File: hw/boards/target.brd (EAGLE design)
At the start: 25.4 x 25.4 mm, 21 parts, among them T1 771-BC847BS-T/R, U1 579-MCP1703T-3002ECB, U2 771-LPC824M201JDH20J, U4 579-MCP6291T-E/OT, X1 798-DF134P125V20

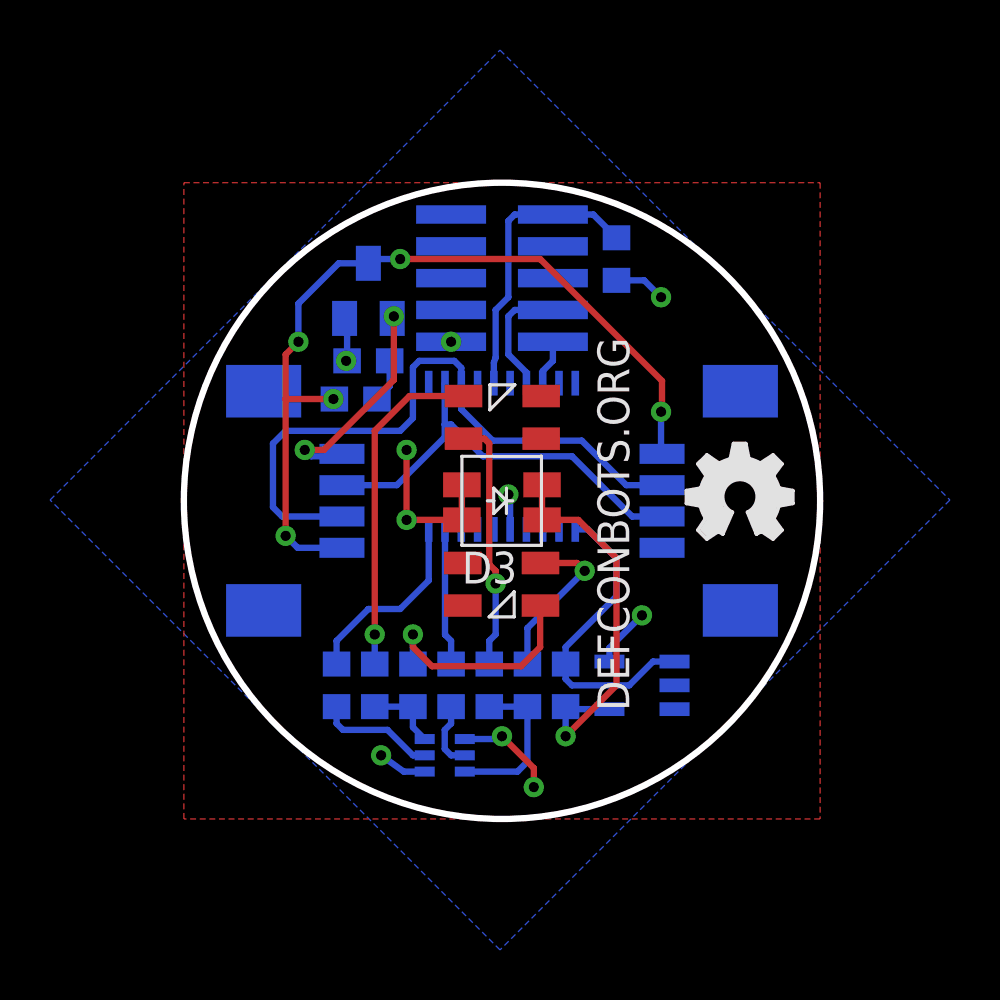
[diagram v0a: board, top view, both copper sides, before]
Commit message: Cleanup some routing. Fix some part numbers
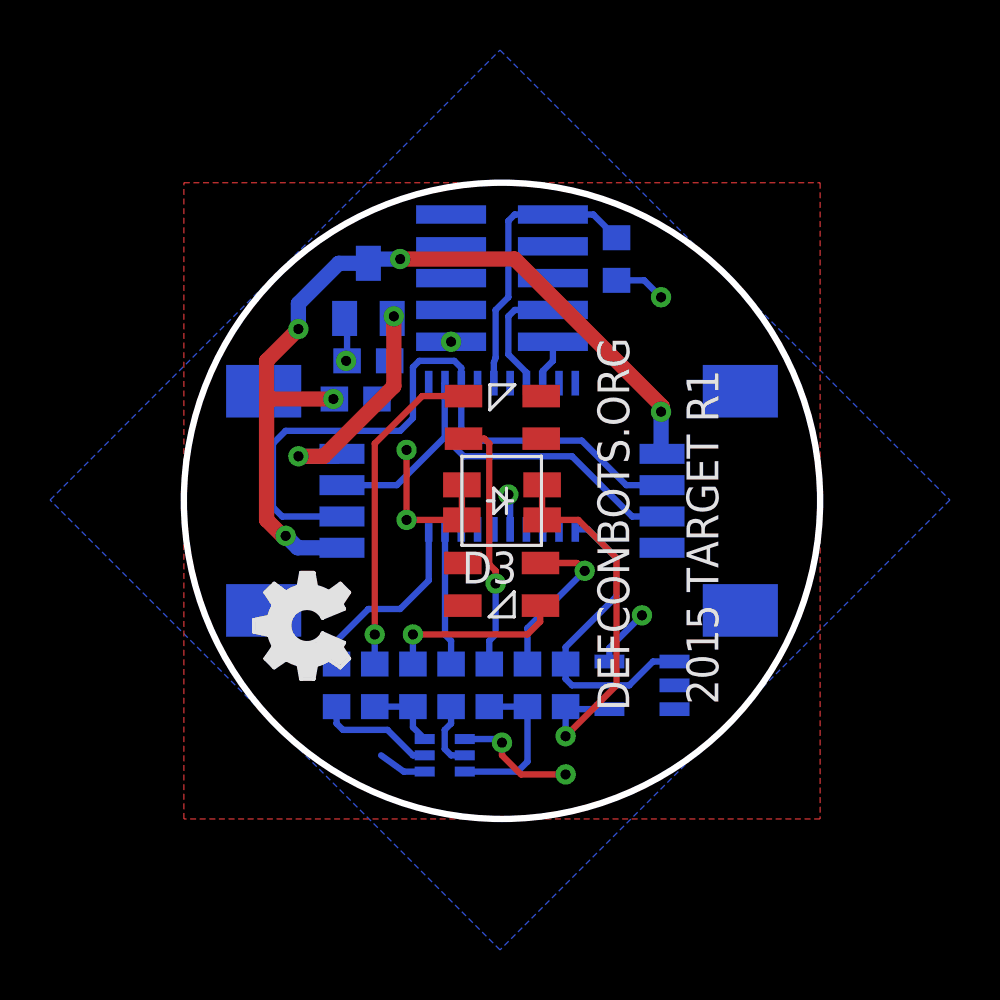
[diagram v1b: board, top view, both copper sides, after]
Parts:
- moved LOGO2 14.6 mm to (6.60, 5.59), turned to 90 degrees
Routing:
- net N$3: track 9.07 -> 7.12 mm
- net GND: track 23.2 -> 24.7 mm, vias 7 -> 6
- net VIN: track 34.3 -> 35.2 mm
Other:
- board text added: "2015 TARGET R1"
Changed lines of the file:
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@@
 <plain>
 <circle x="12.7" y="12.7" radius="12.7" width="0.254" layer="20"/>
-<text x="17.78" y="4.318" size="1.27" layer="21" rot="R90">DEFCONBOTS.ORG</text>
+<text x="17.78" y="4.318" size="1.27" layer="21" font="vector" rot="R90">DEFCONBOTS.ORG</text>
+<text x="21.336" y="4.572" size="1.27" layer="21" font="vector" rot="R90">2015 TARGET R1</text>
 </plain>
 <attributes>
@@
 </element>
 <element name="JP2" library="torpedo" package="FTSH-105-01-XXX-DV-K" value="FTSH-105-01-L" x="12.7" y="21.59" rot="MR90"/>
-<element name="LOGO2" library="ohw-logo" package="OSHW_FILLX150_NOTEXT" value="OSHW_LOGO_FILLX0150-NT" x="20.066" y="11.176"/>
+<element name="LOGO2" library="ohw-logo" package="OSHW_FILLX150_NOTEXT" value="OSHW_LOGO_FILLX0150-NT" x="6.604" y="5.588" rot="R90"/>
 <element name="R1" library="rcl" package="R0603" value="71-CRCW0603-5.6-E3" x="13.716" y="5.334" rot="MR90"/>
 <element name="R11" library="rcl" package="R0603" value="71-CRCW060368R0FKEB" x="9.144" y="5.334" rot="MR90"/>
@@
 <wire x1="9.614" y1="1.89" x2="8.778" y2="1.89" width="0.254" layer="16"/>
 <wire x1="8.778" y1="1.89" x2="7.874" y2="2.54" width="0.254" layer="16"/>
-<via x="7.874" y="2.54" extent="1-16" drill="0.4064"/>
 <wire x1="11.0998" y1="11.938" x2="8.89" y2="11.938" width="0.254" layer="1"/>
 <via x="8.89" y="11.938" extent="1-16" drill="0.4064"/>
@@
 <wire x1="11.0998" y1="11.938" x2="11.0998" y2="13.338" width="0.254" layer="1"/>
 <wire x1="11.214" y1="3.19" x2="12.588" y2="3.19" width="0.254" layer="16"/>
-<wire x1="12.588" y1="3.19" x2="12.7" y2="3.302" width="0.254" layer="16"/>
-<via x="12.7" y="3.302" extent="1-16" drill="0.4064"/>
-<via x="13.97" y="1.27" extent="1-16" drill="0.4064"/>
-<wire x1="12.7" y1="3.302" x2="13.97" y2="2.032" width="0.254" layer="1"/>
-<wire x1="13.97" y1="2.032" x2="13.97" y2="1.27" width="0.254" layer="1"/>
+<wire x1="12.588" y1="3.19" x2="12.7" y2="3.048" width="0.254" layer="16"/>
+<via x="12.7" y="3.048" extent="1-16" drill="0.4064"/>
+<via x="15.24" y="1.778" extent="1-16" drill="0.4064"/>
+<wire x1="12.7" y1="3.048" x2="12.7" y2="2.54" width="0.254" layer="1"/>
+<wire x1="12.7" y1="2.54" x2="13.462" y2="1.778" width="0.254" layer="1"/>
+<wire x1="13.462" y1="1.778" x2="15.24" y2="1.778" width="0.254" layer="1"/>
 <wire x1="8.89" y1="14.732" x2="8.89" y2="11.938" width="0.254" layer="1"/>
-<wire x1="8.382" y1="17.526" x2="8.382" y2="20.066" width="0.254" layer="1"/>
-<wire x1="5.588" y1="14.732" x2="8.382" y2="17.526" width="0.254" layer="1"/>
-<wire x1="4.826" y1="14.732" x2="5.588" y2="14.732" width="0.254" layer="1"/>
-<wire x1="5.08" y1="14.478" x2="4.826" y2="14.732" width="0.254" layer="16"/>
-<wire x1="6.096" y1="14.478" x2="5.08" y2="14.478" width="0.254" layer="16"/>
+<wire x1="8.382" y1="17.272" x2="8.382" y2="20.066" width="0.6096" layer="1"/>
+<wire x1="5.588" y1="14.478" x2="8.382" y2="17.272" width="0.6096" layer="1"/>
+<wire x1="4.572" y1="14.478" x2="5.588" y2="14.478" width="0.6096" layer="1"/>
+<wire x1="6.096" y1="14.478" x2="4.572" y2="14.478" width="0.6096" layer="16"/>
 <wire x1="6.096" y1="14.478" x2="6.31" y2="14.575" width="0.254" layer="16"/>
 <via x="8.382" y="20.066" extent="1-16" drill="0.4064"/>
-<via x="4.826" y="14.732" extent="1-16" drill="0.4064"/>
+<via x="4.572" y="14.478" extent="1-16" drill="0.4064"/>
 <wire x1="7.708" y1="16.764" x2="8.216" y2="17.272" width="0.254" layer="16"/>
 <wire x1="8.216" y1="17.272" x2="8.216" y2="18.288" width="0.254" layer="16"/>
@@
 <contactref element="JP1" pad="1"/>
 <contactref element="X1" pad="1"/>
-<wire x1="6.31" y1="10.825" x2="4.542" y2="10.825" width="0.254" layer="16"/>
-<wire x1="4.542" y1="10.825" x2="4.064" y2="11.303" width="0.254" layer="16"/>
+<wire x1="6.31" y1="10.825" x2="4.542" y2="10.825" width="0.6096" layer="16"/>
+<wire x1="4.542" y1="10.825" x2="4.064" y2="11.303" width="0.6096" layer="16"/>
 <via x="4.064" y="11.303" extent="1-16" drill="0.4064"/>
-<wire x1="4.064" y1="11.303" x2="4.064" y2="16.764" width="0.254" layer="1"/>
-<wire x1="4.064" y1="16.764" x2="4.064" y2="18.542" width="0.254" layer="1"/>
-<wire x1="4.064" y1="18.542" x2="4.572" y2="19.05" width="0.254" layer="1"/>
-<via x="4.572" y="19.05" extent="1-16" drill="0.4064"/>
-<wire x1="4.572" y1="19.05" x2="4.572" y2="20.574" width="0.254" layer="16"/>
-<wire x1="4.572" y1="20.574" x2="6.18" y2="22.182" width="0.254" layer="16"/>
-<wire x1="8.636" y1="22.352" x2="7.366" y2="22.352" width="0.254" layer="16"/>
+<wire x1="4.064" y1="11.303" x2="3.937" y2="11.303" width="0.254" layer="1"/>
+<wire x1="3.937" y1="11.303" x2="3.302" y2="11.938" width="0.6096" layer="1"/>
+<wire x1="3.302" y1="11.938" x2="3.302" y2="16.764" width="0.6096" layer="1"/>
+<wire x1="3.302" y1="16.764" x2="3.302" y2="18.288" width="0.6096" layer="1"/>
+<wire x1="3.302" y1="18.288" x2="4.572" y2="19.558" width="0.6096" layer="1"/>
+<via x="4.572" y="19.558" extent="1-16" drill="0.4064"/>
+<wire x1="4.572" y1="19.558" x2="4.572" y2="20.574" width="0.6096" layer="16"/>
+<wire x1="4.572" y1="20.574" x2="6.18" y2="22.182" width="0.6096" layer="16"/>
+<wire x1="8.636" y1="22.352" x2="7.366" y2="22.352" width="0.6096" layer="16"/>
 <wire x1="7.366" y1="22.352" x2="7.366" y2="22.182" width="0.254" layer="16"/>
 <wire x1="19.05" y1="14.732" x2="19.09" y2="14.575" width="0.254" layer="16"/>
 <via x="8.636" y="22.352" extent="1-16" drill="0.4064"/>
-<wire x1="8.636" y1="22.352" x2="14.224" y2="22.352" width="0.254" layer="1"/>
-<wire x1="14.224" y1="22.352" x2="19.09" y2="17.486" width="0.254" layer="1"/>
-<wire x1="19.09" y1="17.486" x2="19.09" y2="16.296" width="0.254" layer="1"/>
+<wire x1="8.636" y1="22.352" x2="13.208" y2="22.352" width="0.6096" layer="1"/>
+<wire x1="13.208" y1="22.352" x2="19.09" y2="16.47" width="0.6096" layer="1"/>
+<wire x1="19.09" y1="16.47" x2="19.09" y2="16.296" width="0.6096" layer="1"/>
 <wire x1="19.09" y1="16.296" x2="19.05" y2="16.256" width="0.254" layer="1"/>
 <via x="19.05" y="16.256" extent="1-16" drill="0.4064"/>
-<wire x1="19.05" y1="16.256" x2="19.05" y2="14.615" width="0.254" layer="16"/>
+<wire x1="19.05" y1="16.256" x2="19.05" y2="14.615" width="0.6096" layer="16"/>
 <wire x1="19.05" y1="14.615" x2="19.09" y2="14.575" width="0.254" layer="16"/>
 <via x="5.969" y="16.764" extent="1-16" drill="0.4064"/>
-<wire x1="5.969" y1="16.764" x2="4.064" y2="16.764" width="0.254" layer="1"/>
+<wire x1="5.969" y1="16.764" x2="3.302" y2="16.764" width="0.6096" layer="1"/>
 <wire x1="6.008" y1="16.764" x2="5.969" y2="16.764" width="0.254" layer="16"/>
-<wire x1="6.18" y1="22.182" x2="7.366" y2="22.182" width="0.254" layer="16"/>
+<wire x1="6.18" y1="22.182" x2="7.366" y2="22.182" width="0.6096" layer="16"/>
 </signal>
 <signal name="BLUE_LED">
@@
 <contactref element="X1" pad="2"/>
 <contactref element="U2" pad="3"/>
-<wire x1="11.075" y1="17.3958" x2="11.075" y2="16.357" width="0.254" layer="16"/>
-<wire x1="11.075" y1="16.357" x2="12.329" y2="15.103" width="0.254" layer="16"/>
-<wire x1="12.329" y1="15.103" x2="15.885" y2="15.103" width="0.254" layer="16"/>
+<wire x1="11.075" y1="17.3958" x2="11.075" y2="15.595" width="0.254" layer="16"/>
+<wire x1="11.075" y1="15.595" x2="11.567" y2="15.103" width="0.254" layer="16"/>
+<wire x1="11.567" y1="15.103" x2="15.885" y2="15.103" width="0.254" layer="16"/>
 <wire x1="6.31" y1="12.075" x2="3.927" y2="12.075" width="0.254" layer="16"/>
 <wire x1="3.927" y1="12.075" x2="3.556" y2="12.446" width="0.254" layer="16"/>
@@
 <wire x1="6.31" y1="13.325" x2="8.499" y2="13.325" width="0.254" layer="16"/>
 <wire x1="8.499" y1="13.325" x2="10.414" y2="15.24" width="0.254" layer="16"/>
-<wire x1="10.414" y1="15.24" x2="10.414" y2="15.748" width="0.254" layer="16"/>
-<wire x1="10.414" y1="15.748" x2="10.414" y2="17.3848" width="0.254" layer="16"/>
+<wire x1="10.414" y1="15.24" x2="10.414" y2="17.3848" width="0.254" layer="16"/>
 <wire x1="10.414" y1="17.3848" x2="10.425" y2="17.3958" width="0.254" layer="16"/>
 <wire x1="19.09" y1="12.075" x2="17.897" y2="12.075" width="0.254" layer="16"/>
 <wire x1="17.897" y1="12.075" x2="15.494" y2="14.478" width="0.254" layer="16"/>
-<wire x1="15.494" y1="14.478" x2="11.938" y2="14.478" width="0.254" layer="16"/>
-<wire x1="11.938" y1="14.478" x2="10.668" y2="15.748" width="0.254" layer="16"/>
-<wire x1="10.668" y1="15.748" x2="10.414" y2="15.748" width="0.254" layer="16"/>
+<wire x1="15.494" y1="14.478" x2="11.176" y2="14.478" width="0.254" layer="16"/>
+<wire x1="11.176" y1="14.478" x2="10.414" y2="15.24" width="0.254" layer="16"/>
 </signal>
 <signal name="N$2">
@@
 <via x="9.144" y="7.366" extent="1-16" drill="0.4064"/>
 <wire x1="14.224" y1="8.506" x2="14.236" y2="8.518" width="0.254" layer="1"/>
-<wire x1="14.224" y1="8.506" x2="14.224" y2="6.858" width="0.254" layer="1"/>
-<wire x1="14.224" y1="6.858" x2="13.462" y2="6.096" width="0.254" layer="1"/>
-<wire x1="13.462" y1="6.096" x2="9.906" y2="6.096" width="0.254" layer="1"/>
-<wire x1="9.906" y1="6.096" x2="9.144" y2="6.858" width="0.254" layer="1"/>
-<wire x1="9.144" y1="6.858" x2="9.144" y2="7.366" width="0.254" layer="1"/>
+<wire x1="14.224" y1="8.506" x2="14.224" y2="7.874" width="0.254" layer="1"/>
+<wire x1="14.224" y1="7.874" x2="13.716" y2="7.366" width="0.254" layer="1"/>
+<wire x1="13.716" y1="7.366" x2="9.144" y2="7.366" width="0.254" layer="1"/>
 </signal>
 <signal name="N$6">
@@
 <wire x1="7.62" y1="6.184" x2="7.62" y2="7.366" width="0.254" layer="16"/>
 <via x="7.62" y="7.366" extent="1-16" drill="0.4064"/>
-<wire x1="7.62" y1="7.366" x2="7.62" y2="15.494" width="0.254" layer="1"/>
-<wire x1="7.62" y1="15.494" x2="9.008" y2="16.882" width="0.254" layer="1"/>
-<wire x1="9.008" y1="16.882" x2="11.164" y2="16.882" width="0.254" layer="1"/>
+<wire x1="7.62" y1="7.366" x2="7.62" y2="14.986" width="0.254" layer="1"/>
+<wire x1="7.62" y1="14.986" x2="9.516" y2="16.882" width="0.254" layer="1"/>
+<wire x1="9.516" y1="16.882" x2="11.164" y2="16.882" width="0.254" layer="1"/>
 </signal>
 <signal name="N$7">

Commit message: Cleanup some parts, generate BOM.
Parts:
- removed R11: 71-CRCW060368R0FKEB, rcl:R0603
- removed R9: 71-CRCW06034M64FKEA, rcl:R0603
- added R4: 71-CRCW0603-5.6-E3, rcl:R0603
- added R7: 71-CRCW0603-10K-E3, rcl:R0603
- R1, R3: value 71-CRCW0603-5.6-E3 -> 71-CRCW060368R0FKEB
- R2: value 71-CRCW060368R0FKEB -> 71-CRCW0603-5.6-E3
- R6: value 71-CRCW0603-10K-E3 -> 71-CRCW0603220RFKEB
- R8: value 71-CRCW0603220RFKEB -> 71-CRCW06034M64FKEA
- moved R6 20.4 mm to (6.10, 5.33)
- moved R2 6.10 mm to (13.7, 5.33)
- moved R8 4.57 mm to (15.2, 5.33), turned to 270 degrees
- moved R3 4.57 mm to (7.62, 5.33)
- moved R1 4.57 mm to (9.14, 5.33)
- moved R5 4.57 mm to (10.7, 5.33)
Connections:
- net +3V3: now also R7.1; no longer R6.1
- net BLUE_LED: now also R6.2; no longer R5.2
- net LASER_RX: now also R8.1; no longer R9.1
- net N$1: now also R2.1, R4.1; no longer R1.1, R3.1
- net N$11: now also R5.1; no longer R8.1
- net N$2: now also R1.1, R3.1; no longer R11.1, R2.1
- net N$3: now also R1.2; no longer R11.2
- net N$4: now also R6.1; no longer R5.1
- net N$5: now also R8.2; no longer R9.2
- net N$6: now also R3.2; no longer R2.2
- net N$7: now also R2.2; no longer R1.2
- net N$8: now also R4.2; no longer R3.2
- net RED_LED: now also R5.2; no longer R8.2
- net RST: now also R7.2; no longer R6.2
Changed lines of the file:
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@@
 <element name="JP2" library="torpedo" package="FTSH-105-01-XXX-DV-K" value="FTSH-105-01-L" x="12.7" y="21.59" rot="MR90"/>
 <element name="LOGO2" library="ohw-logo" package="OSHW_FILLX150_NOTEXT" value="OSHW_LOGO_FILLX0150-NT" x="6.604" y="5.588" rot="R90"/>
-<element name="R1" library="rcl" package="R0603" value="71-CRCW0603-5.6-E3" x="13.716" y="5.334" rot="MR90"/>
-<element name="R11" library="rcl" package="R0603" value="71-CRCW060368R0FKEB" x="9.144" y="5.334" rot="MR90"/>
-<element name="R2" library="rcl" package="R0603" value="71-CRCW060368R0FKEB" x="7.62" y="5.334" rot="MR90"/>
-<element name="R3" library="rcl" package="R0603" value="71-CRCW0603-5.6-E3" x="12.192" y="5.334" rot="MR90"/>
-<element name="R5" library="rcl" package="R0603" value="71-CRCW0603220RFKEB" x="6.096" y="5.334" rot="MR90"/>
-<element name="R6" library="rcl" package="R0603" value="71-CRCW0603-10K-E3" x="17.272" y="22.352" rot="MR90"/>
-<element name="R8" library="rcl" package="R0603" value="71-CRCW0603220RFKEB" x="10.668" y="5.334" rot="MR90"/>
-<element name="R9" library="rcl" package="R0603" value="71-CRCW06034M64FKEA" x="15.24" y="5.334" rot="MR270"/>
+<element name="R2" library="rcl" package="R0603" value="71-CRCW0603-5.6-E3" x="13.716" y="5.334" rot="MR90"/>
+<element name="R1" library="rcl" package="R0603" value="71-CRCW060368R0FKEB" x="9.144" y="5.334" rot="MR90"/>
+<element name="R3" library="rcl" package="R0603" value="71-CRCW060368R0FKEB" x="7.62" y="5.334" rot="MR90"/>
+<element name="R4" library="rcl" package="R0603" value="71-CRCW0603-5.6-E3" x="12.192" y="5.334" rot="MR90"/>
+<element name="R6" library="rcl" package="R0603" value="71-CRCW0603220RFKEB" x="6.096" y="5.334" rot="MR90"/>
+<element name="R7" library="rcl" package="R0603" value="71-CRCW0603-10K-E3" x="17.272" y="22.352" rot="MR90"/>
+<element name="R5" library="rcl" package="R0603" value="71-CRCW0603220RFKEB" x="10.668" y="5.334" rot="MR90"/>
+<element name="R8" library="rcl" package="R0603" value="71-CRCW06034M64FKEA" x="15.24" y="5.334" rot="MR270"/>
 <element name="T1" library="transistor-small-signal" package="SOT363_PHILIPS" value="771-BC847BS-T/R" x="10.414" y="2.54" rot="MR90"/>
 <element name="U1" library="linear" package="SOT23" value="579-MCP1703T-3002ECB" x="7.366" y="21.082" rot="MR0"/>
@@
 <contactref element="JP1" pad="4"/>
 <contactref element="X1" pad="4"/>
-<contactref element="U2" pad="16"/>
 <contactref element="JP2" pad="9"/>
 <contactref element="JP2" pad="5"/>
@@
 <wire x1="7.708" y1="16.764" x2="8.216" y2="17.272" width="0.254" layer="16"/>
 <wire x1="8.216" y1="17.272" x2="8.216" y2="18.288" width="0.254" layer="16"/>
+<contactref element="U2" pad="16"/>
 </signal>
 <signal name="+3V3">
@@
 <contactref element="U2" pad="15"/>
 <contactref element="JP2" pad="1"/>
-<contactref element="R6" pad="1"/>
+<contactref element="R7" pad="1"/>
 <wire x1="6.416" y1="19.982" x2="6.516" y2="19.882" width="0.254" layer="16"/>
 <wire x1="6.516" y1="19.882" x2="6.516" y2="18.288" width="0.254" layer="16"/>
@@
 </signal>
 <signal name="BLUE_LED">
-<contactref element="R5" pad="2"/>
+<contactref element="R6" pad="2"/>
 <contactref element="U2" pad="20"/>
 <wire x1="9.775" y1="9.521" x2="9.775" y2="11.5602" width="0.254" layer="16"/>
@@
 </signal>
 <signal name="RED_LED">
-<contactref element="R8" pad="2"/>
+<contactref element="R5" pad="2"/>
 <contactref element="U2" pad="19"/>
 <wire x1="10.425" y1="11.5602" x2="10.425" y2="7.355" width="0.254" layer="16"/>
@@
 </signal>
 <signal name="N$5">
-<contactref element="R9" pad="2"/>
+<contactref element="R8" pad="2"/>
 <contactref element="U4" pad="4"/>
 <contactref element="D3" pad="3"/>
@@
 </signal>
 <signal name="LASER_RX">
-<contactref element="R9" pad="1"/>
+<contactref element="R8" pad="1"/>
 <contactref element="U4" pad="1"/>
 <contactref element="U2" pad="11"/>
@@
 </signal>
 <signal name="N$4">
-<contactref element="R5" pad="1"/>
+<contactref element="R6" pad="1"/>
 <contactref element="T1" pad="2"/>
 <wire x1="9.614" y1="2.54" x2="9.144" y2="2.54" width="0.254" layer="16"/>
@@
 </signal>
 <signal name="N$11">
-<contactref element="R8" pad="1"/>
+<contactref element="R5" pad="1"/>
 <contactref element="T1" pad="5"/>
 <wire x1="10.668" y1="4.484" x2="10.668" y2="3.81" width="0.254" layer="16"/>
@@
 <contactref element="U2" pad="5"/>
 <contactref element="JP2" pad="10"/>
-<contactref element="R6" pad="2"/>
+<contactref element="R7" pad="2"/>
 <wire x1="14.732" y1="24.13" x2="16.344" y2="24.13" width="0.254" layer="16"/>
 <wire x1="16.344" y1="24.13" x2="17.272" y2="23.202" width="0.254" layer="16"/>
@@
 <signal name="N$2">
 <contactref element="T1" pad="3"/>
-<contactref element="R11" pad="1"/>
-<contactref element="R2" pad="1"/>
+<contactref element="R1" pad="1"/>
+<contactref element="R3" pad="1"/>
 <wire x1="7.62" y1="4.484" x2="9.144" y2="4.484" width="0.254" layer="16"/>
 <wire x1="9.144" y1="4.484" x2="9.144" y2="3.66" width="0.254" layer="16"/>
@@
 <signal name="N$3">
 <contactref element="D1" pad="3"/>
-<contactref element="R11" pad="2"/>
+<contactref element="R1" pad="2"/>
 <wire x1="9.144" y1="6.184" x2="9.144" y2="7.366" width="0.254" layer="16"/>
 <via x="9.144" y="7.366" extent="1-16" drill="0.4064"/>
@@
 <signal name="N$6">
 <contactref element="D2" pad="3"/>
-<contactref element="R2" pad="2"/>
+<contactref element="R3" pad="2"/>
 <wire x1="7.62" y1="6.184" x2="7.62" y2="7.366" width="0.254" layer="16"/>
 <via x="7.62" y="7.366" extent="1-16" drill="0.4064"/>
@@
 <signal name="N$7">
 <contactref element="D1" pad="4"/>
-<contactref element="R1" pad="2"/>
+<contactref element="R2" pad="2"/>
 <wire x1="13.716" y1="6.184" x2="13.716" y2="7.62" width="0.254" layer="16"/>
 <wire x1="13.716" y1="7.62" x2="16.002" y2="9.906" width="0.254" layer="16"/>
@@
 <signal name="N$8">
 <contactref element="D2" pad="4"/>
-<contactref element="R3" pad="2"/>
+<contactref element="R4" pad="2"/>
 <wire x1="11.164" y1="15.182" x2="11.996" y2="15.182" width="0.254" layer="1"/>
 <via x="12.446" y="9.398" extent="1-16" drill="0.4064"/>
@@
 </signal>
 <signal name="N$1">
-<contactref element="R3" pad="1"/>
+<contactref element="R4" pad="1"/>
 <contactref element="T1" pad="6"/>
-<contactref element="R1" pad="1"/>
+<contactref element="R2" pad="1"/>
 <wire x1="12.192" y1="4.484" x2="13.716" y2="4.484" width="0.254" layer="16"/>
 <wire x1="11.214" y1="1.89" x2="13.32" y2="1.89" width="0.254" layer="16"/>
